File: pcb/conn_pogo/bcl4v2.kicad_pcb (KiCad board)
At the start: 2 copper layers, 35.5 x 6 mm, 3 parts, among them J1 Conn_01x05, J2 Conn_01x05, J3 Conn_01x05

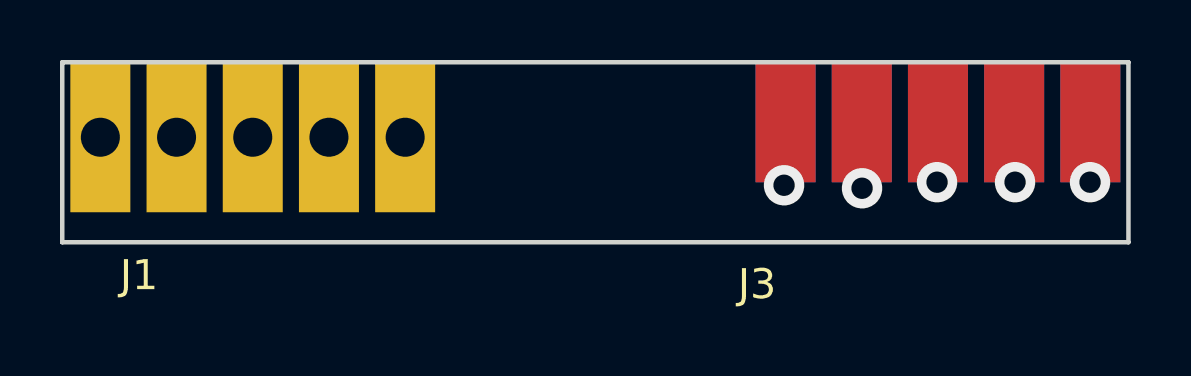
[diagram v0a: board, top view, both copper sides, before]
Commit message: - make larger holes for pogo pins
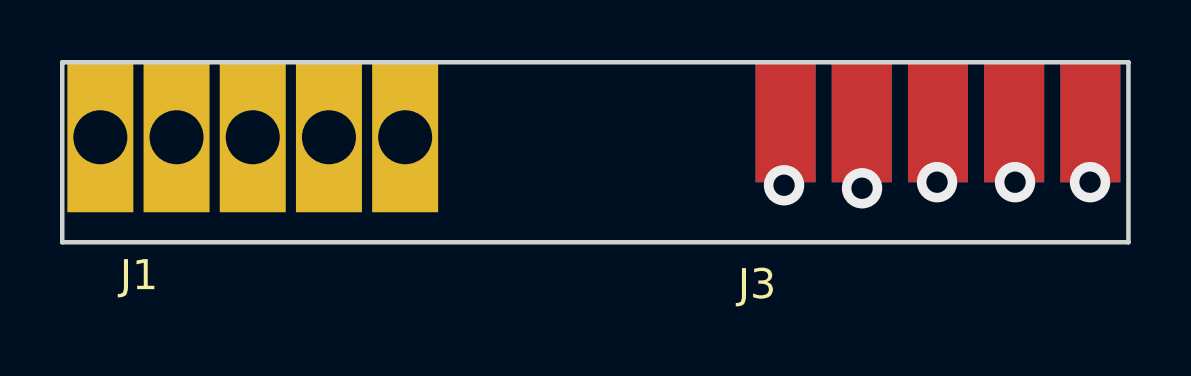
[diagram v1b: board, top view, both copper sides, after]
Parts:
- J1: footprint libraries:5way_pogo_1mm_hole -> libraries:5way_pogo_1.5mm_hole
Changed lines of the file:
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@@
     (add_net "Net-(J2-Pad5)")
-  )
-  (module libraries:5way_pogo_1mm_hole (layer Front)
-    (at 83.51 102.5)
-    (fp_text reference J1 (at 1.29 4.6) (layer F.SilkS)
-      (effects (font (size 1 1) (thickness 0.15)))
-    )
-    (fp_text value Conn_01x05 (at 5.715 -3.81) (layer F.Fab)
-      (effects (font (size 1 1) (thickness 0.15)))
-    )
-    (pad 5 thru_hole rect (at 10.16 0) (size 2 5) (drill 1.3) (layers *.Cu *.Mask)
-      (net 1 "Net-(J1-Pad5)"))
-    (pad 4 thru_hole rect (at 7.62 0) (size 2 5) (drill 1.3) (layers *.Cu *.Mask)
-      (net 2 "Net-(J1-Pad4)"))
-    (pad 3 thru_hole rect (at 5.08 0) (size 2 5) (drill 1.3) (layers *.Cu *.Mask)
-      (net 3 "Net-(J1-Pad3)"))
-    (pad 2 thru_hole rect (at 2.54 0) (size 2 5) (drill 1.3) (layers *.Cu *.Mask)
-      (net 4 "Net-(J1-Pad2)"))
-    (pad 1 thru_hole rect (at 0 0) (size 2 5) (drill 1.3) (layers *.Cu *.Mask)
-      (net 5 "Net-(J1-Pad1)"))
   )
   (module libraries:5way_pogo_pad (layer Back)
@@
       (net 10 "Net-(J2-Pad1)"))
   )
+  (module libraries:5way_pogo_1.5mm_hole (layer Front)
+    (at 83.51 102.5)
+    (fp_text reference J1 (at 1.29 4.6) (layer F.SilkS)
+      (effects (font (size 1 1) (thickness 0.15)))
+    )
+    (fp_text value Conn_01x05 (at 5.715 -3.81) (layer F.Fab)
+      (effects (font (size 1 1) (thickness 0.15)))
+    )
+    (pad 1 thru_hole rect (at 0 0) (size 2.2 5) (drill 1.8) (layers *.Cu *.Mask)
+      (net 5 "Net-(J1-Pad1)"))
+    (pad 2 thru_hole rect (at 2.54 0) (size 2.2 5) (drill 1.8) (layers *.Cu *.Mask)
+      (net 4 "Net-(J1-Pad2)"))
+    (pad 3 thru_hole rect (at 5.08 0) (size 2.2 5) (drill 1.8) (layers *.Cu *.Mask)
+      (net 3 "Net-(J1-Pad3)"))
+    (pad 4 thru_hole rect (at 7.62 0) (size 2.2 5) (drill 1.8) (layers *.Cu *.Mask)
+      (net 2 "Net-(J1-Pad4)"))
+    (pad 5 thru_hole rect (at 10.16 0) (size 2.2 5) (drill 1.8) (layers *.Cu *.Mask)
+      (net 1 "Net-(J1-Pad5)"))
+  )
   (gr_line (start 82.24 100) (end 82.24 106) (layer Edge.Cuts) (width 0.15))
